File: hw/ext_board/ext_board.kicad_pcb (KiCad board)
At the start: 2 copper layers, 63.5 x 55.9 mm, 60 parts, among them J1 Conn_01x03, J2 Conn_01x05, J3 Conn_01x03, J4 Conn_01x02, Q1 SS8050, Q2 SS8050, Q3 SS8050, Q4 SS8050, Q5 SS8050, Q6 SS8050, Q7 SS8050, Q8 SS8050, Q9 SS8050, U1 74HC595PW, U2 74HC595PW, U3 M24LC16, U4 M93C76, X1 UNO_R3_CONN

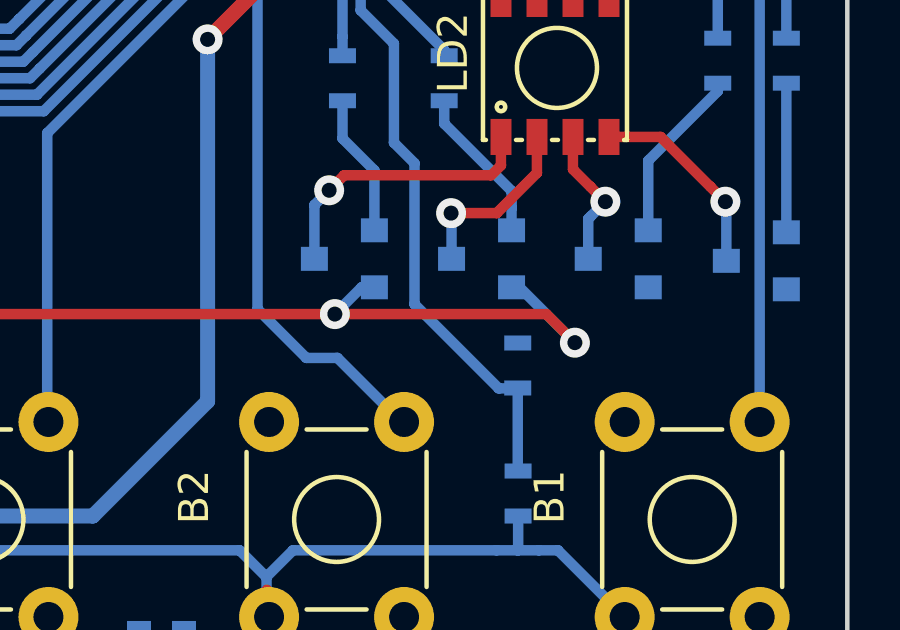
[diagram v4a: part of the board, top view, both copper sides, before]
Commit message: Add diodes to buttons
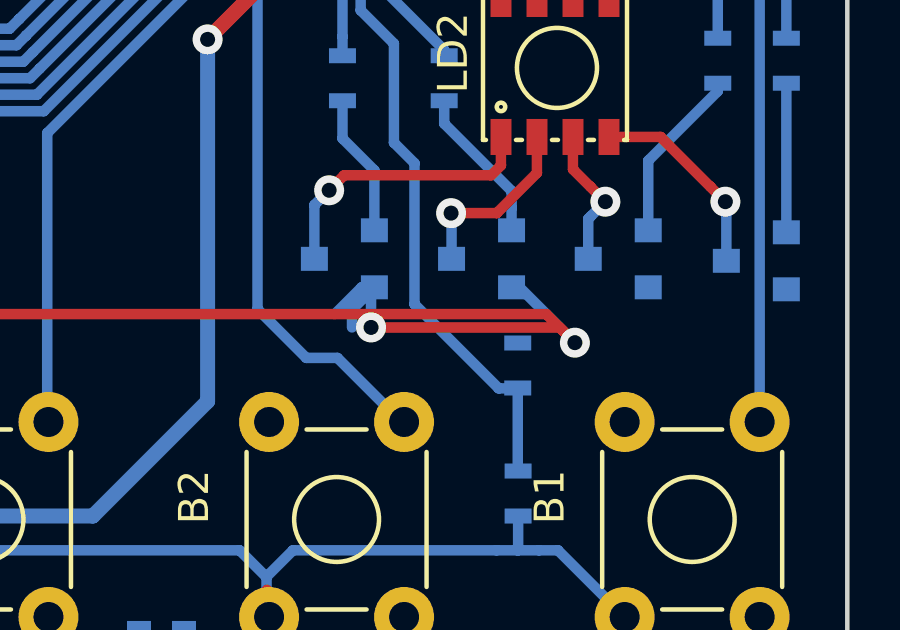
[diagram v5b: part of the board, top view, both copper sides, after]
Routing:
- net GND: track 232.6 -> 242.6 mm
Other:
- board text added: "A0"
- board text added: "A1"
- board text added: "A2"
- board text added: "A3"
- board text added: "A4"
- board text added: "A5"
- board text added: "AVDD"
- board text added: "CLK"
- board text added: "CS"
- board text added: "D0"
- board text added: "D1"
- board text added: "D10"
- board text added: "D11"
- board text added: "D12"
- board text added: "D13"
- board text added: "D14"
- board text added: "D15"
- board text added: "D2"
- board text added: "D3"
- board text added: "D4"
- board text added: "D5"
- board text added: "D6"
- board text added: "D7"
- board text added: "D8"
- board text added: "D9"
- board text added: "GND"
- board text added: "MISO"
- board text added: "MOSI"
- board text added: "RX"
- board text added: "SCK"
- board text added: "SDA"
- board text added: "TX"
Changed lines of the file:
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@@
     (links 139)
     (no_connects 0)
-    (area 110.484367 54.45 189.095953 115.974219)
+    (area 110.484367 54.45 189.095953 116.927142)
     (thickness 1.6)
-    (drawings 22)
-    (tracks 682)
+    (drawings 58)
+    (tracks 688)
     (zones 0)
     (modules 60)
@@
   (page A4)
   (layers
-    (0 F.Cu signal)
-    (31 B.Cu signal)
-    (32 B.Adhes user)
+    (0 F.Cu signal hide)
+    (31 B.Cu signal hide)
+    (32 B.Adhes user hide)
     (33 F.Adhes user)
-    (34 B.Paste user)
-    (35 F.Paste user)
-    (36 B.SilkS user)
+    (34 B.Paste user hide)
+    (35 F.Paste user hide)
+    (36 B.SilkS user hide)
     (37 F.SilkS user)
-    (38 B.Mask user)
-    (39 F.Mask user)
-    (40 Dwgs.User user)
-    (41 Cmts.User user)
+    (38 B.Mask user hide)
+    (39 F.Mask user hide)
+    (40 Dwgs.User user hide)
+    (41 Cmts.User user hide)
     (42 Eco1.User user)
-    (43 Eco2.User user)
+    (43 Eco2.User user hide)
     (44 Edge.Cuts user)
-    (45 Margin user)
-    (46 B.CrtYd user)
-    (47 F.CrtYd user)
-    (48 B.Fab user)
-    (49 F.Fab user)
+    (45 Margin user hide)
+    (46 B.CrtYd user hide)
+    (47 F.CrtYd user hide)
+    (48 B.Fab user hide)
+    (49 F.Fab user hide)
   )
   (setup
@@
     (pad_to_mask_clearance 0.2)
     (aux_axis_origin 121.92 114.3)
-    (visible_elements FFFFFFFF)
+    (visible_elements FFFC1FFF)
     (pcbplotparams
-      (layerselection 0x00000_80000001)
+      (layerselection 0x01480_00000000)
       (usegerberextensions false)
       (excludeedgelayer false)
@@
       (psnegative false)
       (psa4output false)
-      (plotreference true)
-      (plotvalue true)
+      (plotreference false)
+      (plotvalue false)
       (plotinvisibletext false)
       (padsonsilk false)
       (subtractmaskfromsilk false)
-      (outputformat 3)
+      (outputformat 1)
       (mirror false)
-      (drillshape 2)
+      (drillshape 0)
       (scaleselection 1)
-      (outputdirectory cam/))
+      (outputdirectory cam/222))
   )
   (net 0 "")
@@
     (pad 3 thru_hole circle (at 0 4.5 90) (size 2 2) (drill 1) (layers *.Cu *.Mask))
   )
+  (gr_text D1 (at 172.72 59.055 90) (layer Eco1.User)
+    (effects (font (size 1.5 1.5) (thickness 0.3)))
+  )
+  (gr_text D0 (at 175.26 59.055 90) (layer Eco1.User)
+    (effects (font (size 1.5 1.5) (thickness 0.3)))
+  )
+  (gr_text D2 (at 170.18 59.055 90) (layer Eco1.User)
+    (effects (font (size 1.5 1.5) (thickness 0.3)))
+  )
+  (gr_text D3 (at 167.64 59.055 90) (layer Eco1.User)
+    (effects (font (size 1.5 1.5) (thickness 0.3)))
+  )
+  (gr_text D6 (at 160.02 59.055 90) (layer Eco1.User)
+    (effects (font (size 1.5 1.5) (thickness 0.3)))
+  )
+  (gr_text D5 (at 162.56 59.055 90) (layer Eco1.User)
+    (effects (font (size 1.5 1.5) (thickness 0.3)))
+  )
+  (gr_text D7 (at 157.48 59.055 90) (layer Eco1.User)
+    (effects (font (size 1.5 1.5) (thickness 0.3)))
+  )
+  (gr_text D9 (at 151.13 59.055 90) (layer Eco1.User)
+    (effects (font (size 1.5 1.5) (thickness 0.3)))
+  )
+  (gr_text D8 (at 153.67 59.055 90) (layer Eco1.User)
+    (effects (font (size 1.5 1.5) (thickness 0.3)))
+  )
+  (gr_text D11 (at 146.05 58.42 90) (layer Eco1.User)
+    (effects (font (size 1.5 1.5) (thickness 0.3)))
+  )
+  (gr_text D4 (at 165.1 59.055 90) (layer Eco1.User)
+    (effects (font (size 1.5 1.5) (thickness 0.3)))
+  )
+  (gr_text D10 (at 148.59 58.42 90) (layer Eco1.User)
+    (effects (font (size 1.5 1.5) (thickness 0.3)))
+  )
+  (gr_text D15 (at 130.81 58.42 90) (layer Eco1.User)
+    (effects (font (size 1.5 1.5) (thickness 0.3)))
+  )
+  (gr_text AVDD (at 135.89 57.785 90) (layer Eco1.User)
+    (effects (font (size 1.5 1.5) (thickness 0.3)))
+  )
+  (gr_text D14 (at 133.35 58.42 90) (layer Eco1.User)
+    (effects (font (size 1.5 1.5) (thickness 0.3)))
+  )
+  (gr_text GND (at 138.43 58.42 90) (layer Eco1.User)
+    (effects (font (size 1.5 1.5) (thickness 0.3)))
+  )
+  (gr_text D13 (at 140.97 58.42 90) (layer Eco1.User)
+    (effects (font (size 1.5 1.5) (thickness 0.3)))
+  )
+  (gr_text D12 (at 143.51 58.42 90) (layer Eco1.User)
+    (effects (font (size 1.5 1.5) (thickness 0.3)))
+  )
+  (gr_text "A5\n" (at 175.895 115.57 90) (layer Eco1.User)
+    (effects (font (size 1.5 1.5) (thickness 0.3)))
+  )
+  (gr_text A4 (at 173.101 115.57 90) (layer Eco1.User)
+    (effects (font (size 1.5 1.5) (thickness 0.3)))
+  )
+  (gr_text A3 (at 170.307 115.57 90) (layer Eco1.User)
+    (effects (font (size 1.5 1.5) (thickness 0.3)))
+  )
+  (gr_text A2 (at 167.513 115.57 90) (layer Eco1.User)
+    (effects (font (size 1.5 1.5) (thickness 0.3)))
+  )
+  (gr_text A1 (at 164.719 115.57 90) (layer Eco1.User)
+    (effects (font (size 1.5 1.5) (thickness 0.3)))
+  )
+  (gr_text A0 (at 161.925 115.57 90) (layer Eco1.User)
+    (effects (font (size 1.5 1.5) (thickness 0.3)))
+  )
+  (gr_text GND (at 185.42 63.5) (layer Eco1.User)
+    (effects (font (size 1.5 1.5) (thickness 0.3)))
+  )
+  (gr_text TX (at 184.785 66.04) (layer Eco1.User)
+    (effects (font (size 1.5 1.5) (thickness 0.3)))
+  )
+  (gr_text RX (at 184.785 68.58) (layer Eco1.User)
+    (effects (font (size 1.5 1.5) (thickness 0.3)))
+  )
+  (gr_text GND (at 133.35 111.125) (layer Eco1.User)
+    (effects (font (size 1.5 1.5) (thickness 0.3)))
+  )
+  (gr_text CLK (at 123.19 92.71) (layer Eco1.User)
+    (effects (font (size 1.5 1.5) (thickness 0.3)))
+  )
+  (gr_text "SDA\n" (at 123.19 95.25) (layer Eco1.User)
+    (effects (font (size 1.5 1.5) (thickness 0.3)))
+  )
+  (gr_text "GND\n" (at 123.19 97.79) (layer Eco1.User)
+    (effects (font (size 1.5 1.5) (thickness 0.3)))
+  )
+  (gr_text "GND\n" (at 136.525 97.79) (layer Eco1.User)
+    (effects (font (size 1.5 1.5) (thickness 0.3)))
+  )
+  (gr_text MISO (at 137.16 95.25) (layer Eco1.User)
+    (effects (font (size 1.5 1.5) (thickness 0.3)))
+  )
+  (gr_text MOSI (at 137.16 92.71) (layer Eco1.User)
+    (effects (font (size 1.5 1.5) (thickness 0.3)))
+  )
+  (gr_text SCK (at 136.525 90.17) (layer Eco1.User)
+    (effects (font (size 1.5 1.5) (thickness 0.3)))
+  )
+  (gr_text CS (at 135.89 87.63) (layer Eco1.User)
+    (effects (font (size 1.5 1.5) (thickness 0.3)))
+  )
   (gr_line (start 120.65 60.96) (end 123.19 60.96) (layer Edge.Cuts) (width 0.1))
   (gr_line (start 121.92 59.69) (end 121.92 62.23) (layer Edge.Cuts) (width 0.1))
@@
   (gr_line (start 182.88 63.5) (end 182.88 111.76) (layer Edge.Cuts) (width 0.15))
   (gr_line (start 124.46 60.96) (end 180.34 60.96) (layer Edge.Cuts) (width 0.15))
+  (segment (start 167.005 97.79) (end 173.2915 97.79) (width 0.35) (layer F.Cu) (net 1))
+  (segment (start 173.2915 97.79) (end 173.7995 98.298) (width 0.35) (layer F.Cu) (net 1))
+  (segment (start 167.005 97.79) (end 167.005 96.565) (width 0.35) (layer B.Cu) (net 1))
+  (segment (start 167.005 96.565) (end 167.116 96.454) (width 0.35) (layer B.Cu) (net 1))
+  (segment (start 166.37 97.79) (end 166.37 97.2) (width 0.35) (layer B.Cu) (net 1))
+  (segment (start 166.37 97.2) (end 167.116 96.454) (width 0.35) (layer B.Cu) (net 1))
   (segment (start 162.5346 67.423) (end 162.6121 67.5005) (width 0.35) (layer F.Cu) (net 1))
   (segment (start 171.5135 67.5005) (end 172.212 68.199) (width 0.35) (layer F.Cu) (net 1))
@@
   (segment (start 167.116 96.454) (end 166.69 96.454) (width 0.35) (layer B.Cu) (net 1))
   (segment (start 166.69 96.454) (end 165.7985 97.3455) (width 0.35) (layer B.Cu) (net 1))
-  (via (at 165.7985 97.3455) (size 1) (drill 0.5) (layers F.Cu B.Cu) (net 1))
+  (via (at 167.005 97.79) (size 1) (drill 0.5) (layers F.Cu B.Cu) (net 1))
   (segment (start 127 105.41) (end 127 111.2139) (width 0.35) (layer B.Cu) (net 1))
   (segment (start 127 111.2139) (end 127.0127 111.2266) (width 0.35) (layer B.Cu) (net 1))
